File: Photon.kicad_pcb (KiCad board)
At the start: 4 copper layers, 21.1 x 83.8 mm, 27 parts, among them SW1 TS-1088-AR02016, SW2 TS-1088-AR02016, U1 ATtiny13A-S, U2 RT8059GJ5, U3 BCR421UW6-7, U4 BCR421UW6-7

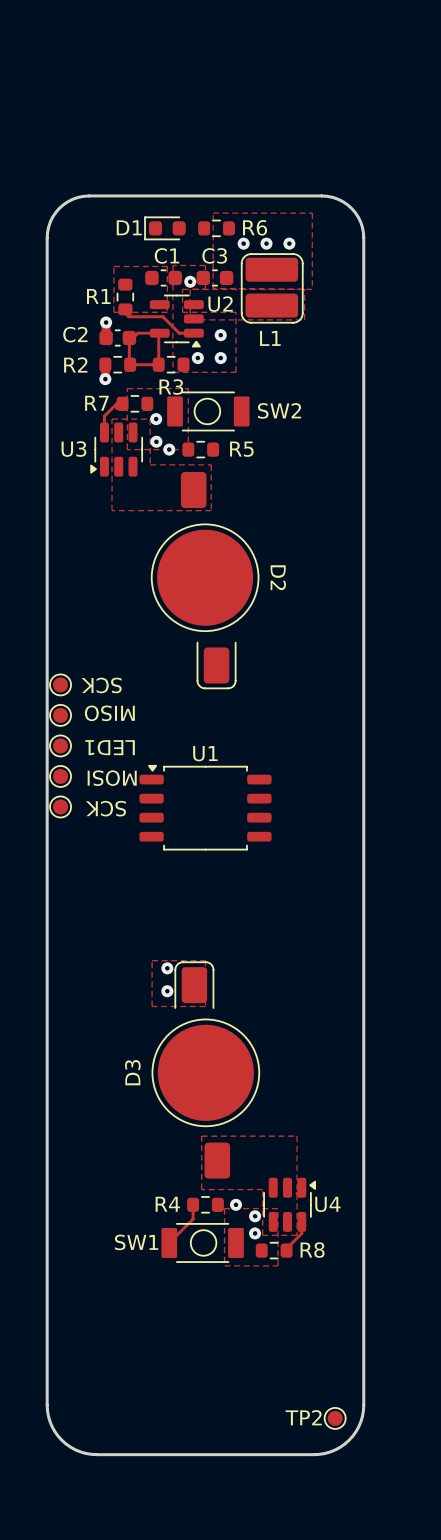
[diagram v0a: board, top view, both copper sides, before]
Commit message: made new pcb. and updated schematic
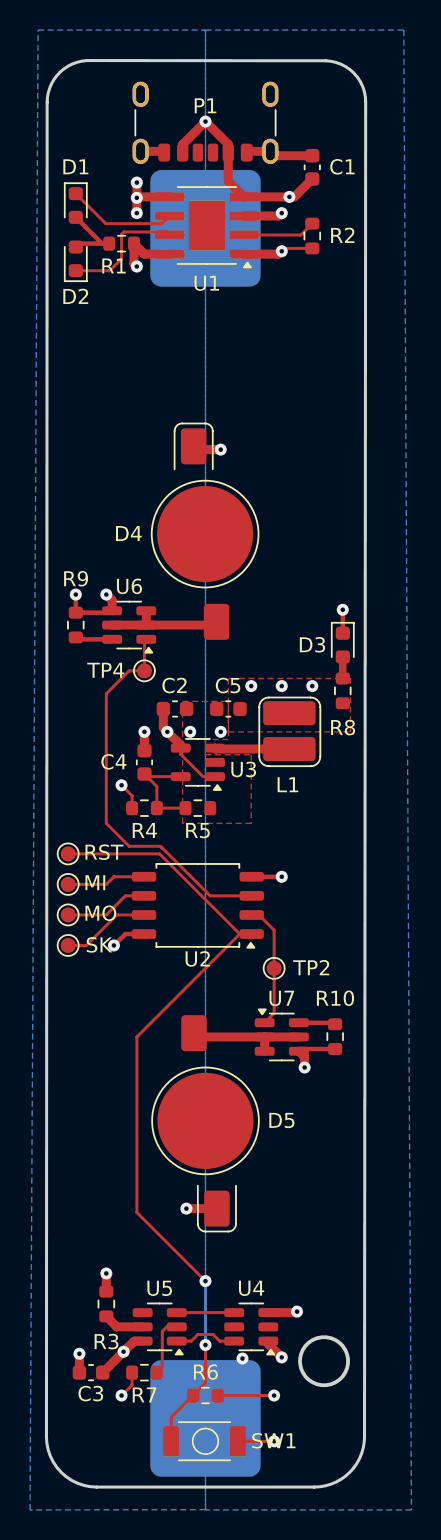
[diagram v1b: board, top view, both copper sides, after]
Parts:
- removed SW2: TS-1088-AR02016, Photon:5mm Push Button
- added BT1: Battery_Cell, Photon:18650 Battery Holder, B.Cu at (52.8, 31.5)
- added C4: 10pF, Capacitor_SMD:C_0603_1608Metric, F.Cu at (48.8, 67.1)
- added C5: 10uF, Capacitor_SMD:C_0603_1608Metric, F.Cu at (54.4, 63.5)
- added D2: SZYY0603R1, LED_SMD:LED_0603_1608Metric, F.Cu at (44.2, 33.5)
- added D3: SZYY0603R1, LED_SMD:LED_0603_1608Metric, F.Cu at (62.0, 59.2)
- added P1: USB_C_6Pin, Connector_USB:USB_C_Receptacle_GCT_USB4125-xx-x-0190_6P_TopMnt_Horizontal, F.Cu at (52.8, 23.4)
- added R10: 20R, Resistor_SMD:R_0603_1608Metric, F.Cu at (61.5, 85.3)
- added R9: 20R, Resistor_SMD:R_0603_1608Metric, F.Cu at (44.2, 57.9)
- added U5: DW01A, Package_TO_SOT_SMD:SOT-23-6, F.Cu at (49.8, 104.6)
- added U6: BCR421UW6-7, Package_TO_SOT_SMD:SOT-23-6, F.Cu at (47.8, 57.9)
- added U7: BCR421UW6-7, Package_TO_SOT_SMD:SOT-23-6, F.Cu at (57.9, 85.3)
- C1: value 4.7uF -> 100nF
- C2: value 10pF -> 4.7uF
- C3: value 10uF -> 100nF
- R1: value 0R -> 2K
- R2: value 500K -> 1K2
- R3: value 100K -> 100R
- R4: value 10K -> 500K
- R5: value 10K -> 100K
- R6: value 300 -> 10K
- R7: value 6.65 -> 1K
- R8: value 6.65 -> 300
- U1: value ATtiny13A-S -> TP4056; footprint Package_SO:SOIC-8_5.3x5.3mm_P1.27mm -> Package_SO:SOIC-8-1EP_3.9x4.9mm_P1.27mm_EP2.41x3.3mm
- U2: value RT8059GJ5 -> ATtiny13A-S; footprint Package_TO_SOT_SMD:SOT-23-5 -> Package_SO:SOIC-8_5.3x5.3mm_P1.27mm
- U3: value BCR421UW6-7 -> RT8059GJ5; footprint Package_TO_SOT_SMD:SOT-23-6 -> Package_TO_SOT_SMD:SOT-23-5
- U4: value BCR421UW6-7 -> FS8205A
- moved R6 77.7 mm to (52.8, 109.2)
- moved C3 73.4 mm to (45.2, 107.7), turned to 180 degrees
- moved R7 64.5 mm to (48.8, 107.7)
- moved R3 62.7 mm to (46.2, 103.1), turned to -90 degrees
- moved U2 39.1 mm to (52.3, 76.6)
- moved U1 38.8 mm to (52.9, 31.3), turned to 180 degrees
- moved R8 37.6 mm to (62.0, 62.3), turned to 90 degrees
- moved TP2 30.2 mm to (57.4, 80.8)
- moved L1 29.6 mm to (58.3, 65.0)
- moved R4 26.7 mm to (48.8, 70.1), turned to 0 degrees
- moved C2 25.0 mm to (50.8, 63.5)
- moved R5 23.9 mm to (52.3, 70.1)
- moved U3 21.5 mm to (52.3, 67.1), turned to 180 degrees
- moved TP1 17.4 mm to (43.7, 79.2), turned to 180 degrees
- moved R2 15.5 mm to (59.9, 32.0), turned to -90 degrees
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- renumbered D2 to D4, D3 to D5
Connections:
- C1 pad 2: /+BAT -> VCC
- C2 pad 1: /FB -> GND
- C2 pad 2: /3V6 -> +BATT
- C3 pad 1: GND -> -BATT
- C3 pad 2: /3V6 -> +BATT
- D1 pad 1: GND -> /USB_PRST
- R1 pad 1: /+BAT -> VCC
- R1 pad 2: /EN -> Net-(D1-A)
- R2 pad 1: /3V6 -> Net-(U1-PROG)
- R2 pad 2: /FB -> GND
- R3 pad 1: /FB -> +BATT
- R3 pad 2: GND -> Net-(U5-VCC)
- R4 pad 2: /MISO_BTN2 -> /FB
- R5 pad 1: /3V6 -> /FB
- R5 pad 2: /RESET_BTN1 -> GND
- R6 pad 2: Net-(D1-A) -> /RESET_BTN1
- R7 pad 1: /Rext1 -> GND
- R7 pad 2: GND -> Net-(U5-Isense)
- R8 pad 1: /Rext2 -> /3V6
- R8 pad 2: GND -> Net-(D3-A)
- SW1 pad 1: /MISO_BTN2 -> /RESET_BTN1
- TP3 pad 1: /MISO_BTN2 -> /MISO
- U1 pad 1: /RESET_BTN1 -> GND
- U1 pad 2: /LED2_EN -> Net-(U1-PROG)
- U1 pad 3: /LED1_EN -> GND
- U1 pad 4: GND -> VCC
- U1 pad 5: /MOSI -> +BATT
- U1 pad 6: /MISO_BTN2 -> /USB_PRST
- U1 pad 7: /SCK -> /CHRG
- U1 pad 8: /3V6 -> VCC
- U2 pad 1: /EN -> /RESET_BTN1
- U2 pad 2: GND -> /LED2_EN
- U2 pad 3: /LX -> /LED1_EN
- U2 pad 4: /+BAT -> GND
- U2 pad 5: /FB -> /MOSI
- U3 pad 1: /LED1_EN -> +BATT
- U3 pad 2: /OUT_LED1 -> GND
- U3 pad 3: /OUT_LED1 -> /LX
- U3 pad 4: GND -> +BATT
- U3 pad 5: /OUT_LED1 -> /FB
- U4 pad 1: /LED2_EN -> -BATT
- U4 pad 2: /OUT_LED2 -> unconnected-(U4-D1/D2-Pad2)
- U4 pad 3: /OUT_LED2 -> GND
- U4 pad 4: GND -> Net-(U4-G2)
- U4 pad 5: /OUT_LED2 -> unconnected-(U4-D1/D2-Pad5)
- U4 pad 6: /Rext2 -> Net-(U4-G1)
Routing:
- net /RESET_BTN1: track 0.00 -> 53.9 mm, vias 0 -> 2
- net GND: track 0.00 -> 31.8 mm, vias 8 -> 12
- net /LED1_EN: track 0.00 -> 25.6 mm
- net VCC: track 0.00 -> 18.1 mm, vias 0 -> 3
- net +BATT: track 0.00 -> 13.1 mm, vias 0 -> 6
- net -BATT: track 0.00 -> 13.1 mm, vias 0 -> 3
- net /3V6: track 1.99 -> 13.1 mm
- net /CHRG: track 0.00 -> 8.36 mm
- net /LED2_EN: track 0.27 -> 8.34 mm
- net /OUT_LED2: track 0.00 -> 8.03 mm
- net /OUT_LED1: track 0.00 -> 7.99 mm
- net /USB_PRST: track 0.00 -> 7.29 mm
- net /SCK: track 0.00 -> 5.89 mm
- net /LX: track 0.00 -> 5.59 mm
- net /MISO: track 0.00 -> 5.57 mm
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- added copper zone on B.Cu, net +BATT
- added copper zone on B.Cu, net -BATT
- added copper zone on In2.Cu, net VCC
- removed copper zone on F.Cu, net /+BAT
- removed copper zone on F.Cu, net /LX
- removed copper zone on F.Cu, net /OUT_LED1
- removed copper zone on F.Cu, net /OUT_LED2
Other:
- board size 21.1 x 83.8 mm -> 21.3 x 95 mm
- board text added: "MI"
- board text added: "MO"
- board text added: "RST"
- board text added: "SK"
- board text removed: "LED1"
- board text removed: "MISO"
- board text removed: "MOSI"
- board text removed: "SCK"

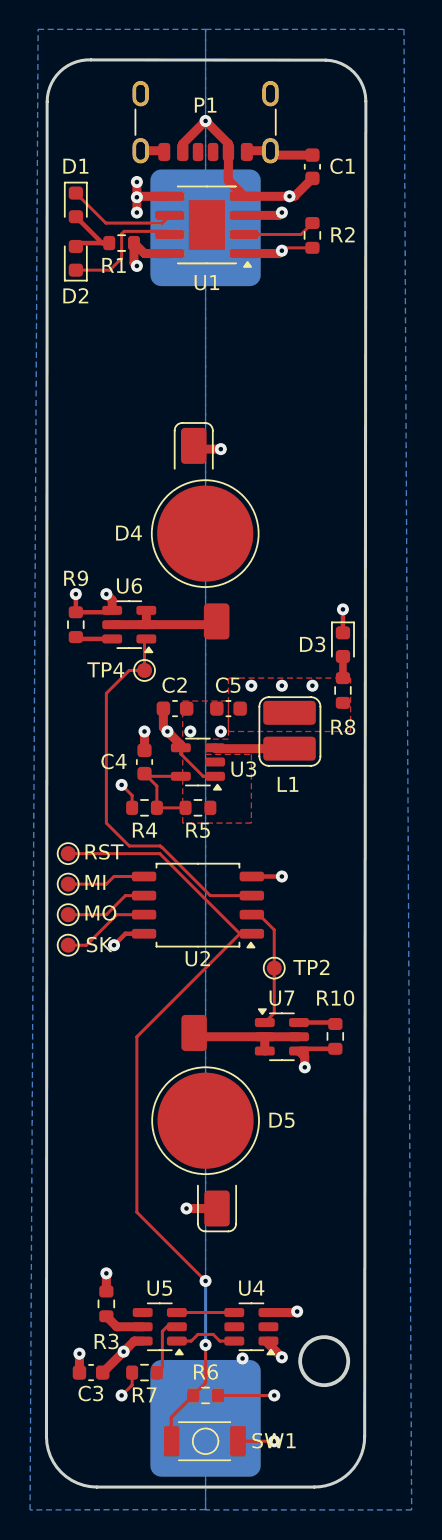
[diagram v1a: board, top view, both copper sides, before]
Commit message: Cleaned up schematic and PCB
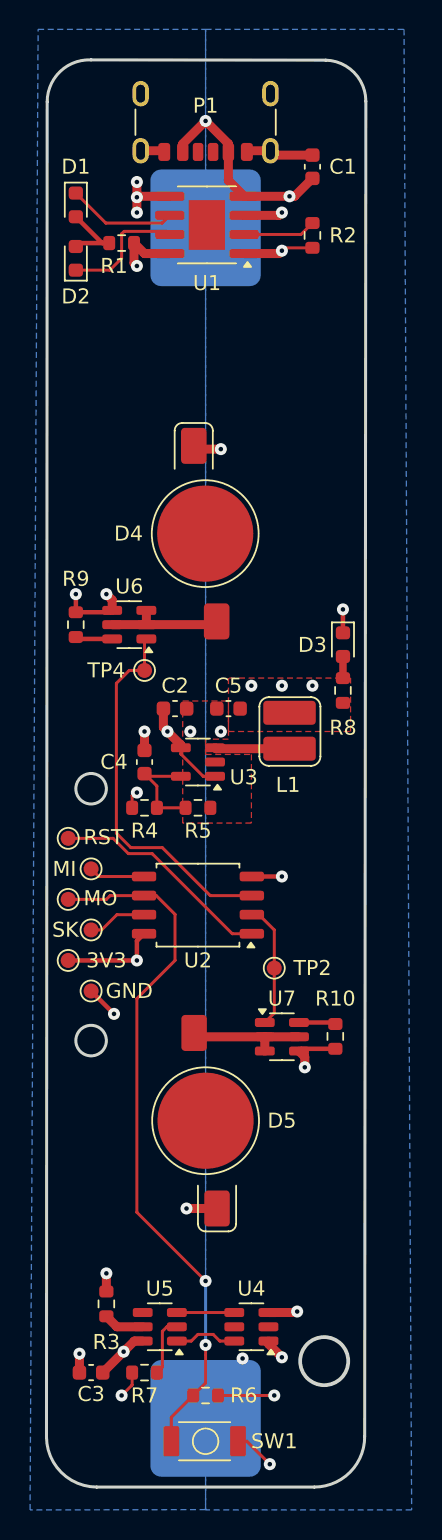
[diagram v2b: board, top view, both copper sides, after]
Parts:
- added TP7: VCC, TestPoint:TestPoint_Pad_D1.0mm, F.Cu at (43.7, 80.3)
- added TP8: GND, TestPoint:TestPoint_Pad_D1.0mm, F.Cu at (45.2, 82.3)
- moved TP1 1.83 mm to (45.2, 78.2)
- moved TP5 1.83 mm to (45.2, 74.2)
- moved TP6 1.02 mm to (43.7, 72.1)
- moved TP3 1.02 mm to (43.7, 76.2)
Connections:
- net /CHRG renamed /!CHRG
- net /USB_PRST renamed /!STDBY
- net Net-(U4-G1) renamed /OD
- net Net-(U4-G2) renamed /OC
- net Net-(U5-Isense) renamed /Isense
- net Net-(U5-VCC) renamed /DW01A_VCC
- R6 pad 2: /RESET_BTN1 -> /MISO_BTN
- SW1 pad 1: /RESET_BTN1 -> /MISO_BTN
- TP3 pad 1: /MISO -> /MISO_BTN
- TP6 pad 1: /RESET_BTN1 -> /RESET
- U2 pad 1: /RESET_BTN1 -> /RESET
- U2 pad 6: /MISO -> /MISO_BTN
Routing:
- net /RESET_BTN1: track 53.9 -> 0.00 mm, vias 2 -> 0
- net /MISO_BTN: track 0.00 -> 46.7 mm, vias 0 -> 2
- net /RESET: track 0.00 -> 14.9 mm
- net /MISO: track 5.57 -> 0.00 mm
- net /3V6: track 13.1 -> 16.7 mm
- net GND: track 31.8 -> 34.3 mm, vias 12 -> 13
- net /SCK: track 5.89 -> 3.95 mm
- net /MOSI: track 5.26 -> 3.73 mm
- net /LED1_EN: track 25.6 -> 25.1 mm
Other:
- outline, holes or cut-outs redrawn
- board text added: "3V3"
- board text added: "GND"

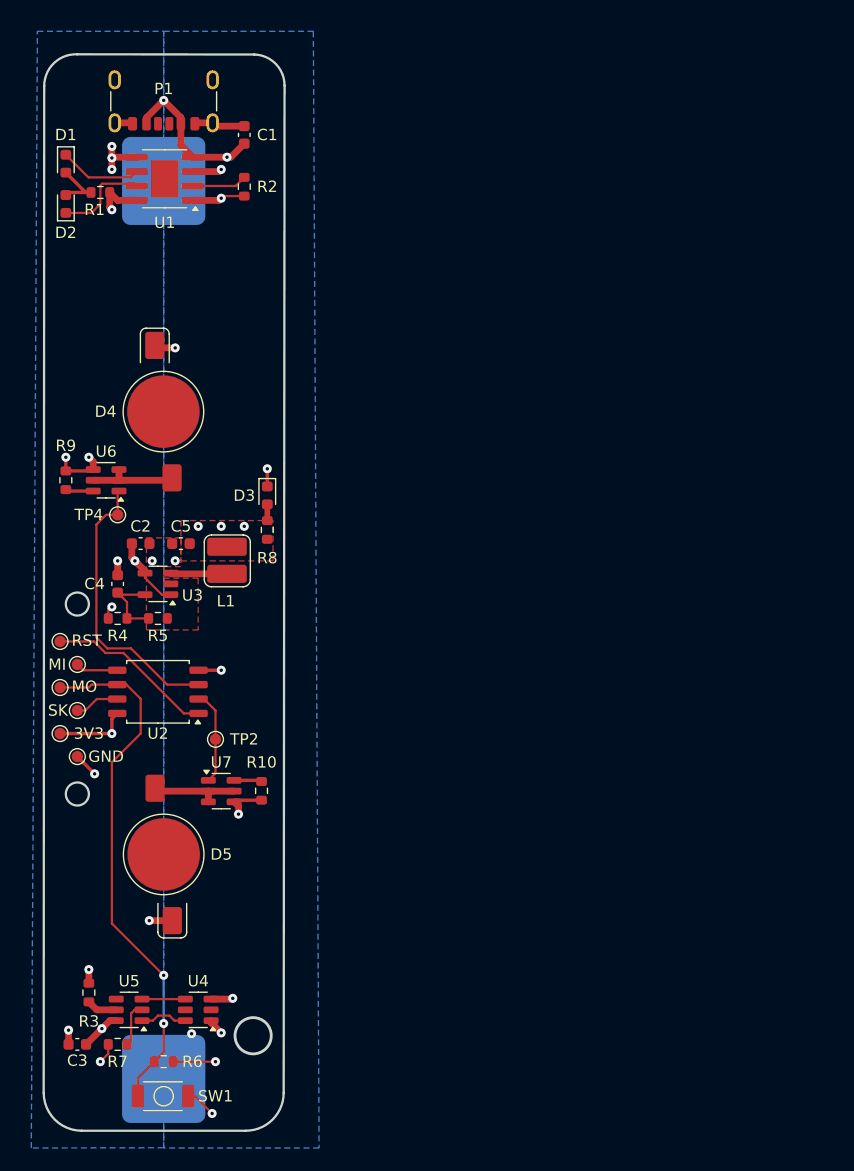
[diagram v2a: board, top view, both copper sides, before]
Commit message: added new ic and started layout
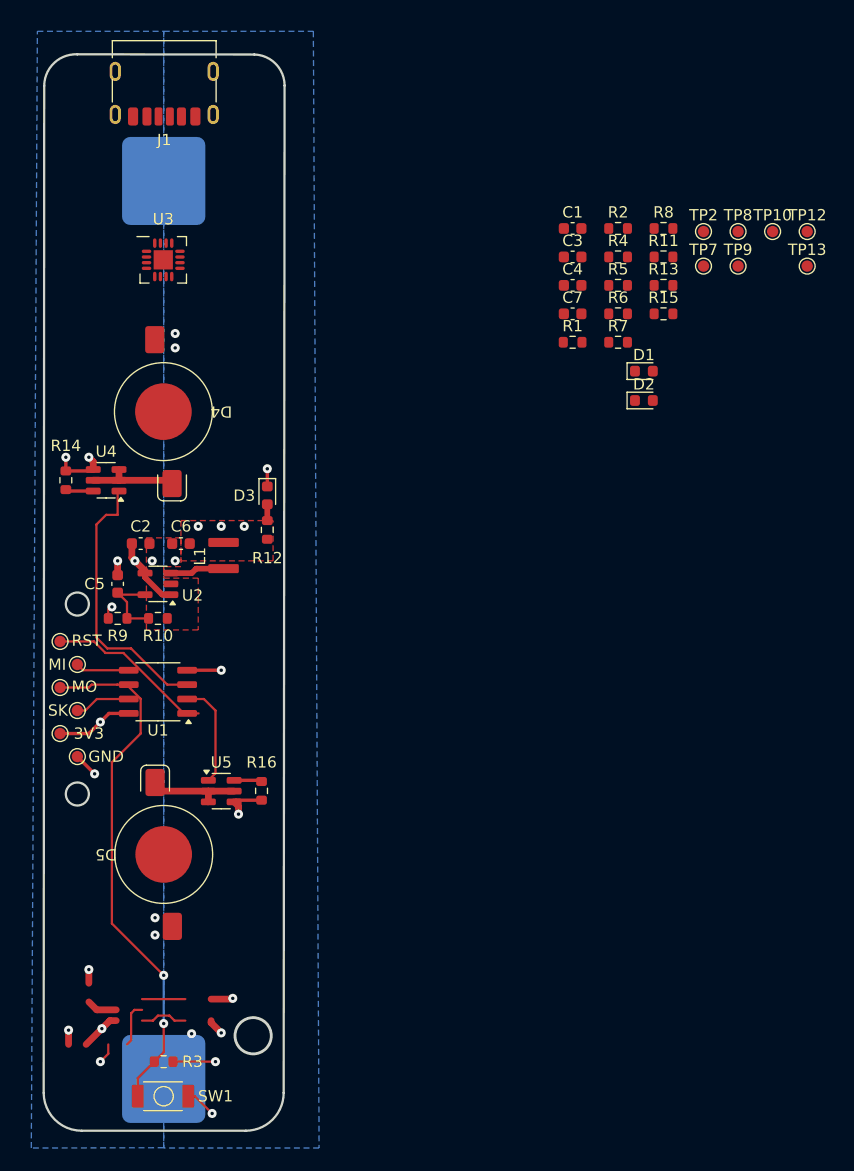
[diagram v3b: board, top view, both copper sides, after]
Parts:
- removed P1: USB_C_6Pin, Connector_USB:USB_C_Receptacle_GCT_USB4125-xx-x-0190_6P_TopMnt_Horizontal
- removed the R3 at (46.2, 103.1)
- removed the TP4 at (48.8, 61.0)
- removed the U1 at (52.9, 31.3)
- removed the U4 at (55.9, 104.6)
- removed the U5 at (49.8, 104.6)
- added C4: 4.7uF, Capacitor_SMD:C_0603_1608Metric, F.Cu at (88.9, 40.7)
- added C7: 4.7uF, Capacitor_SMD:C_0603_1608Metric, F.Cu at (88.9, 43.2)
- added J1: USB_C_Receptacle_USB2.0_14P, Connector_USB:USB_C_Receptacle_HRO_TYPE-C-31-M-17, F.Cu at (52.9, 22.6)
- added R11: 1.18K, Resistor_SMD:R_0603_1608Metric, F.Cu at (96.9, 38.2)
- added R13: 10K, Resistor_SMD:R_0603_1608Metric, F.Cu at (96.9, 40.7)
- added R15: 10K, Resistor_SMD:R_0603_1608Metric, F.Cu at (96.9, 43.2)
- added R4: 10K, Resistor_SMD:R_0603_1608Metric, F.Cu at (92.9, 38.2)
- added R5: 0R, Resistor_SMD:R_0603_1608Metric, F.Cu at (92.9, 40.7)
- added R6: 1K, Resistor_SMD:R_0603_1608Metric, F.Cu at (92.9, 43.2)
- added R8: 1K, Resistor_SMD:R_0603_1608Metric, F.Cu at (96.9, 35.7)
- added TP10: Vout, TestPoint:TestPoint_Pad_D1.0mm, F.Cu at (106.6, 36.0)
- added TP11: 3V6, TestPoint:TestPoint_Pad_D1.0mm, F.Cu at (43.7, 80.3)
- added TP12: LED1_EN, TestPoint:TestPoint_Pad_D1.0mm, F.Cu at (109.6, 36.0)
- added TP13: LED2_EN, TestPoint:TestPoint_Pad_D1.0mm, F.Cu at (109.6, 39.0)
- added TP8: BuckEN, TestPoint:TestPoint_Pad_D1.0mm, F.Cu at (103.5, 36.0)
- added TP9: BAT+, TestPoint:TestPoint_Pad_D1.0mm, F.Cu at (103.5, 39.0)
- added U3: BQ24072RGTR, Photon:QFN-16_EP_3.8x3.8_Pitch0.5mm, F.Cu at (52.8, 38.5)
- C1, C3: value 100nF -> 4.7uF
- L1: value 2.2uH -> 4.7uH; footprint Photon:SMD 3.5x3mm Power Inductor -> Photon:SMD 3x3mm Power Inductor
- R1: value 2K -> 5.1K
- R2: value 1K2 -> 5.1K
- R7: value 1K -> 1.18K
- TP2: value LED2 -> VCC
- TP7: value VCC -> BTN
- U1: renamed from U2; footprint Package_SO:SOIC-8_5.3x5.3mm_P1.27mm -> Package_SO:SO-8_3.9x4.9mm_P1.27mm
- moved C3 82.1 mm to (88.9, 38.2), turned to 0 degrees
- moved R7 76.1 mm to (92.9, 45.7)
- moved TP7 70.2 mm to (100.5, 39.0)
- moved TP2 62.2 mm to (100.5, 36.0)
- moved D1 54.2 mm to (95.2, 48.3), turned to 0 degrees
- moved D2 53.9 mm to (95.2, 50.9), turned to 0 degrees
- moved R1 43.7 mm to (88.9, 45.7), turned to 0 degrees
- moved R2 33.2 mm to (92.9, 35.7), turned to 0 degrees
- moved C1 30.1 mm to (88.9, 35.7), turned to 0 degrees
- moved L1 0.55 mm to (58.0, 64.6)
- turned D4 to -90 degrees
- turned D5 to 90 degrees
- renumbered C4 to C5, C5 to C6, R5 to R10, R8 to R12, R9 to R14, R10 to R16, R6 to R3, R4 to R9, TP8 to TP1, TP6 to TP3, TP5 to TP4, TP3 to TP5, TP1 to TP6, U3 to U2, U6 to U4, U7 to U5
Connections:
- BT1 pad 1: +BATT -> /BAT
- BT1 pad 2: -BATT -> GND
- C1 pad 2: VCC -> /3V6
- C2 pad 2: +BATT -> VOUT
- C3 pad 1: -BATT -> GND
- C3 pad 2: +BATT -> /BAT
- D1 pad 1: /!STDBY -> /PGOOD
- D1 pad 2: Net-(D1-A) -> /G_A
- D2 pad 1: /!CHRG -> /CHG
- D2 pad 2: Net-(D1-A) -> /R_A
- R1 pad 1: VCC -> /CC1
- R1 pad 2: Net-(D1-A) -> GND
- R2 pad 1: Net-(U1-PROG) -> /CC2
- R7 pad 1: GND -> /ILIM
- R7 pad 2: /Isense -> GND
- TP2 pad 1: /LED2_EN -> VCC
- TP7 pad 1: /3V6 -> /MISO_BTN
- U2 pad 1: +BATT -> VOUT
- U2 pad 4: +BATT -> VOUT
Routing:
- net (no net): track 0.00 -> 18.6 mm, vias 0 -> 3
- net VCC: track 18.1 -> 0.00 mm, vias 3 -> 0
- net +BATT: track 13.1 -> 0.00 mm, vias 6 -> 0
- net -BATT: track 13.1 -> 0.00 mm, vias 3 -> 0
- net /!CHRG: track 8.36 -> 0.00 mm
- net /!STDBY: track 7.29 -> 0.00 mm
- net VOUT: track 0.00 -> 6.37 mm, vias 0 -> 1
- net Net-(D1-A): track 5.27 -> 0.00 mm
- net Net-(U1-PROG): track 4.86 -> 0.00 mm
- net /OD: track 4.19 -> 0.00 mm
- net /Isense: track 3.99 -> 0.00 mm
- net /OC: track 3.82 -> 0.00 mm
- net /3V6: track 16.7 -> 13.0 mm, vias 9 -> 11
- net /DW01A_VCC: track 2.71 -> 0.00 mm
- net /SCK: track 3.95 -> 4.96 mm
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- added copper zone on B.Cu, net /BAT
- added copper zone on B.Cu, net GND
- removed copper zone on B.Cu, net +BATT
- removed copper zone on B.Cu, net -BATT
